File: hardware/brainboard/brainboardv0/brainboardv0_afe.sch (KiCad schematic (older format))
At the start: 25 parts, among them U3 OPA2376, U4 ADS1299

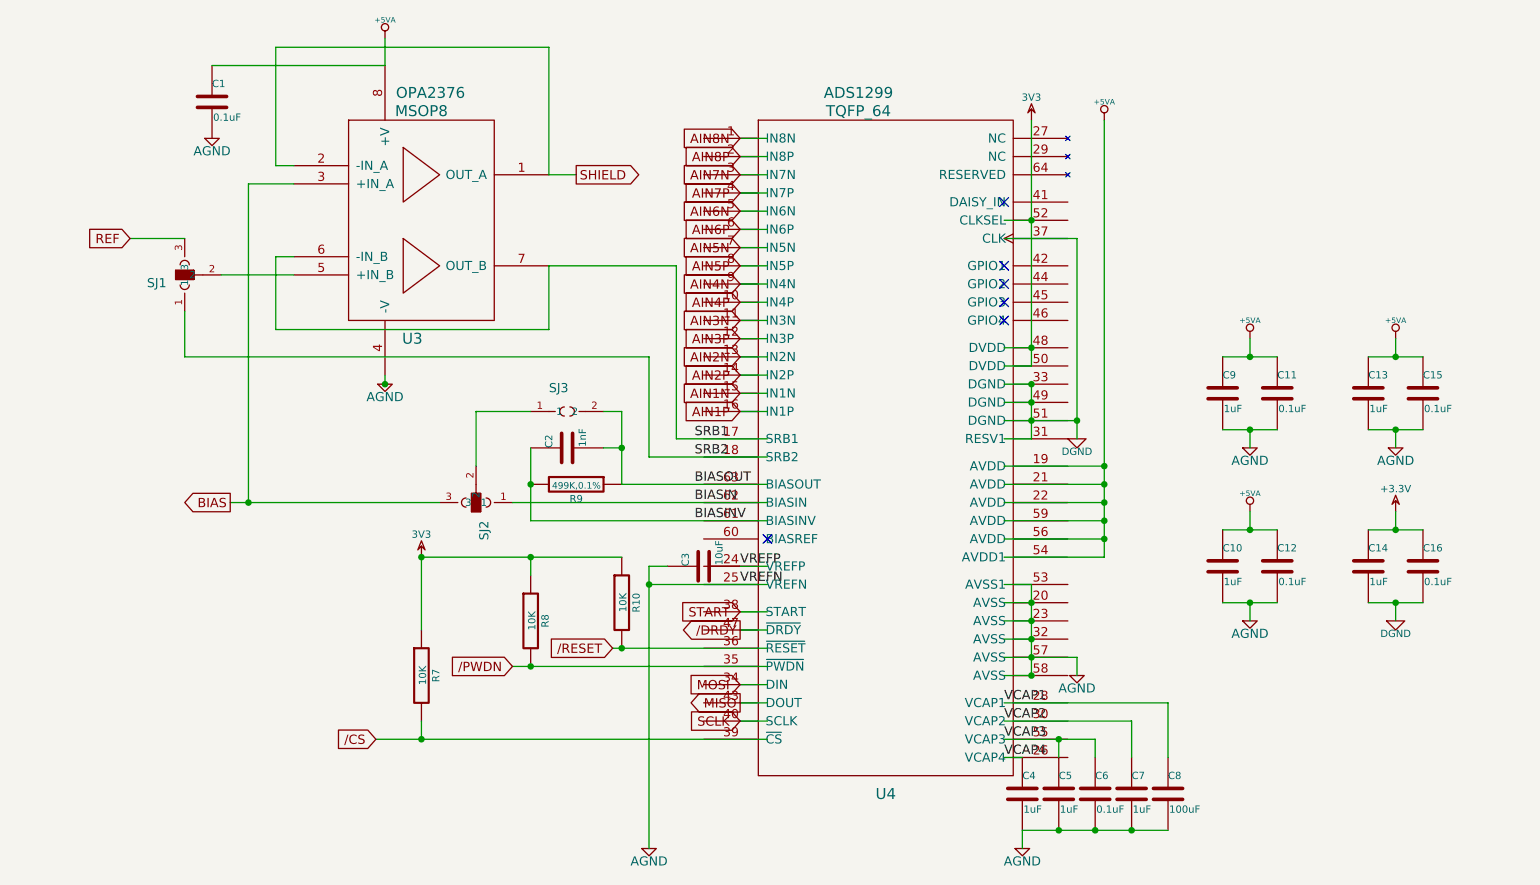
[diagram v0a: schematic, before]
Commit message: Thesis version
Finally able to commit again (Windows XP issues fixed by OS upgrade).
Added latest version of wearable BB, along with prototype "muscleboard"
2-channel board for EMG/ECG applications
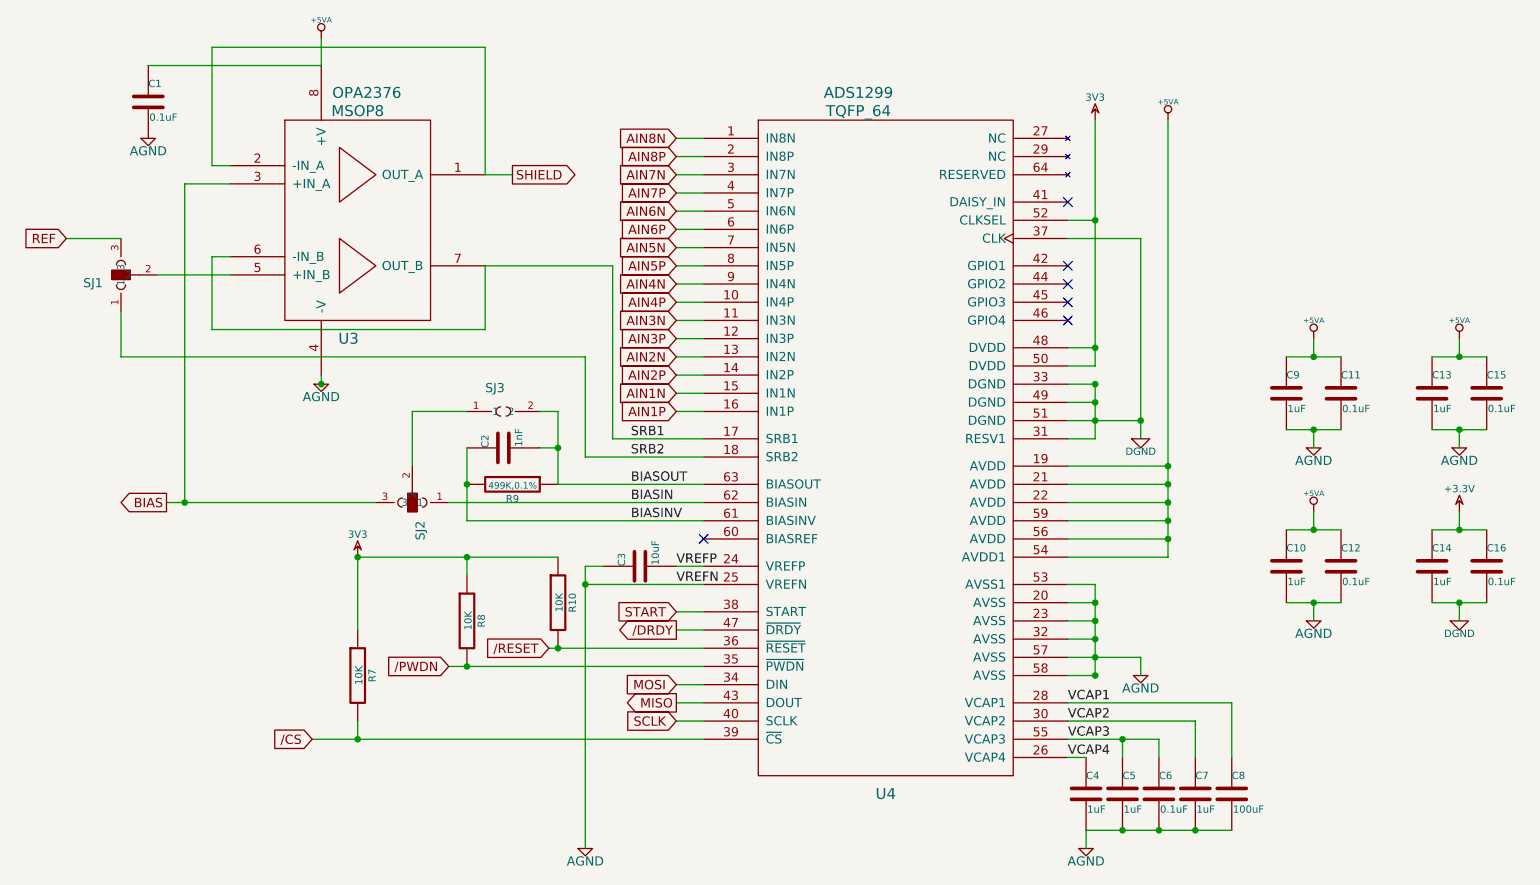
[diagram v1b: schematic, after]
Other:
- moved on the sheet: C1, C10, C11, C12, C13, C14, C15, C16, C2, C3, C4, C5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
